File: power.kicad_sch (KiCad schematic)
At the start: 53 parts, among them J1 USB_C_Receptacle_USB2.0_14P, Q2 Q_NMOS_GDS, SW2 SW_SPDT, U16 74LVC1G125, U2 BQ25895RTW, U4 LM1117DT-3.3, U5 MCP4017-xxxxLT, U7 LM3478MA

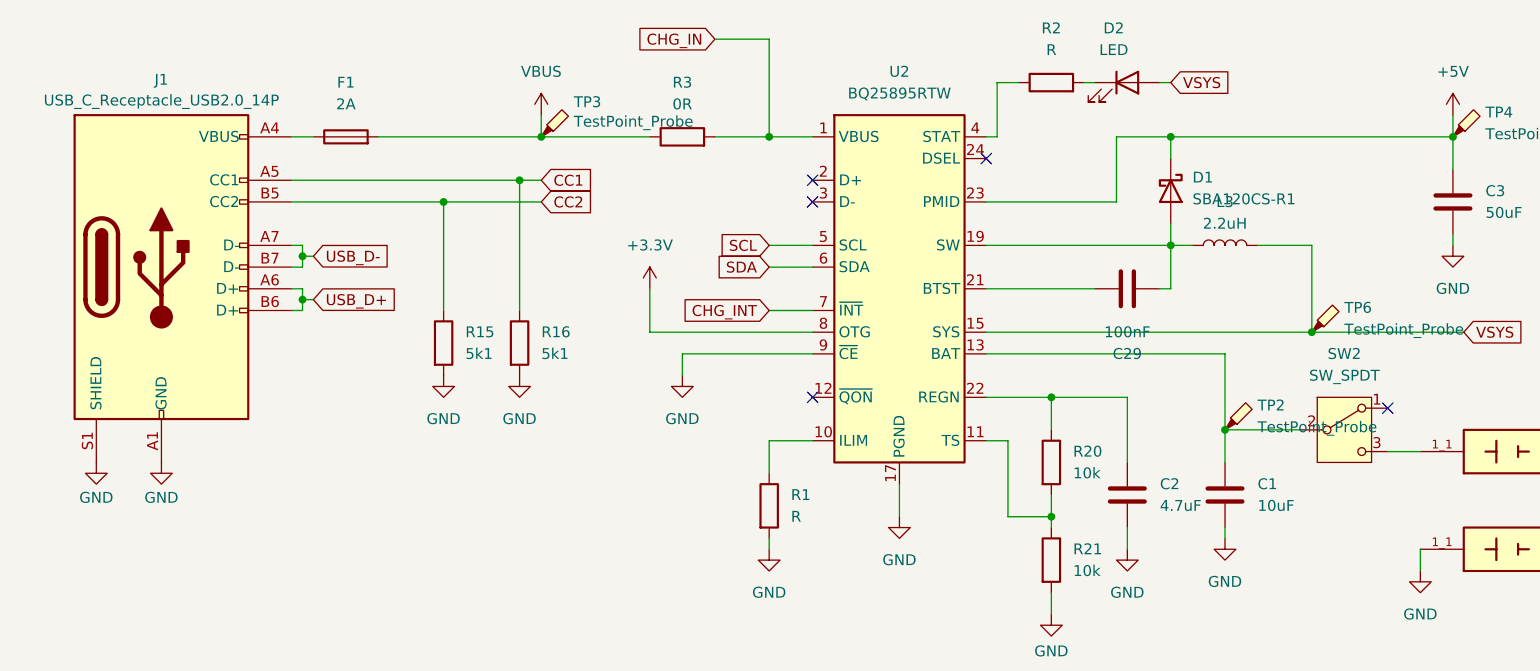
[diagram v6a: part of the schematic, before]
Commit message: Add mounting holes and put test points
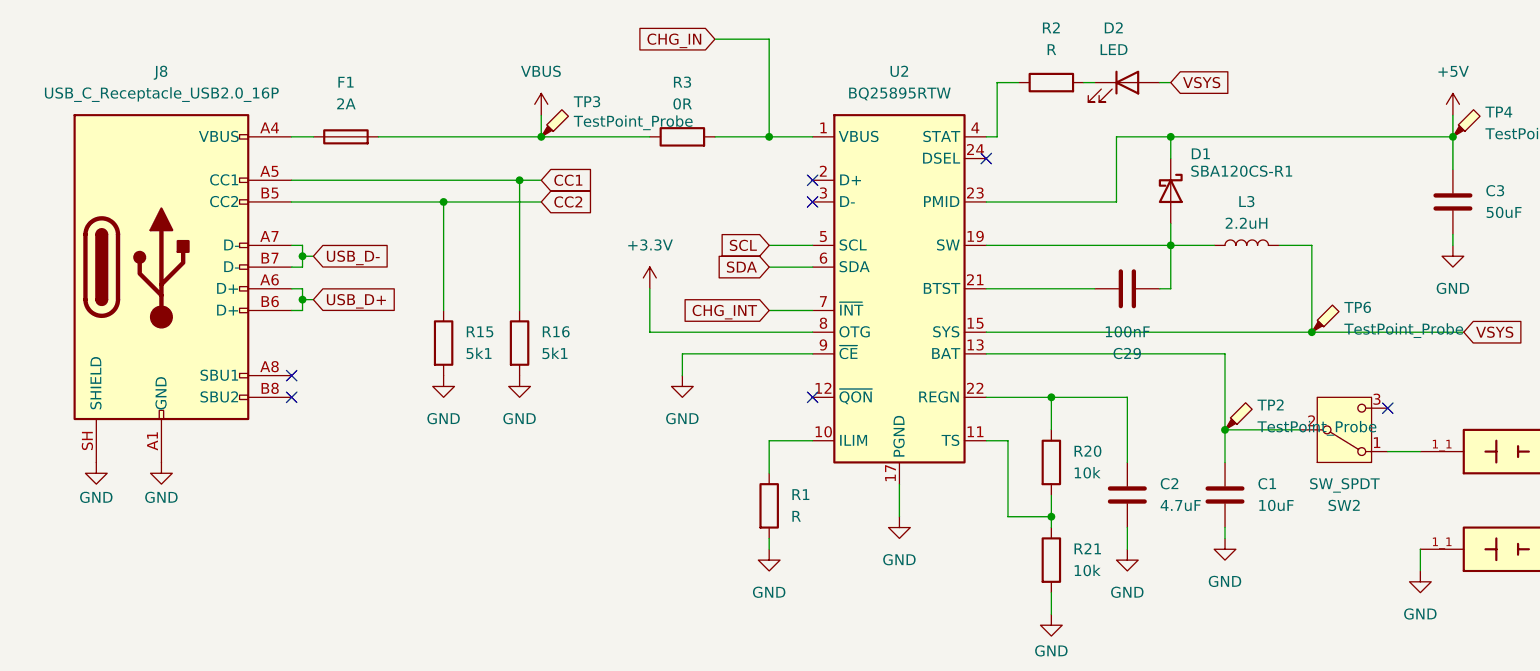
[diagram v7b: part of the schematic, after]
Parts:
- removed J1: USB_C_Receptacle_USB2.0_14P, Connector_USB:USB_C_Receptacle_G-Switch_GT-USB-7010ASV, symbol Connector:USB_C_Receptacle_USB2.0_14P
- added J8: USB_C_Receptacle_USB2.0_16P, Connector_USB:USB_C_Receptacle_G-Switch_GT-USB-7010ASV, symbol Connector:USB_C_Receptacle_USB2.0_16P
- TP2: footprint TestPoint:TestPoint_THTPad_D2.0mm_Drill1.0mm -> TestPoint:TestPoint_Pad_D2.0mm
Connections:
- net CC1: now also J8.A5 (CC1)
- net CC2: now also J8.B5 (CC2)
- net GND: now also J8.A1 (GND), J8.A12 (GND), J8.B1 (GND), J8.B12 (GND), J8.SH (SHIELD)
- net USB_D+: now also J8.A6 (D+), J8.B6 (D+)
- net USB_D-: now also J8.A7 (D-), J8.B7 (D-)
- net at SW2.1 (A): now also BT1.1_1, BT1.1_2, BT1.1_3
- net at F1.1: now also J8.A4 (VBUS), J8.A9 (VBUS), J8.B4 (VBUS), J8.B9 (VBUS)
- now unconnected: SW2.3 (C)
- no-connect marks 6 -> 8
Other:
- moved on the sheet: L3
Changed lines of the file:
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@@
 	)
 	(no_connect
+		(at 48.26 60.96)
+	)
+	(no_connect
 		(at 109.22 60.96)
 	)
@@
 	)
 	(no_connect
+		(at 48.26 58.42)
+	)
+	(no_connect
 		(at 166.37 139.7)
 	)
@@
 	(wire
 		(pts
-			(xy 167.64 43.18) (xy 161.29 43.18)
+			(xy 167.64 43.18) (xy 163.83 43.18)
 		)
 		(stroke
@@
 	(wire
 		(pts
-			(xy 151.13 43.18) (xy 153.67 43.18)
+			(xy 151.13 43.18) (xy 156.21 43.18)
 		)
 		(stroke
@@
 		(in_pos_files yes)
 		(dnp no)
-		(fields_autoplaced yes)
 		(property "Reference" "D1"
-			(at 153.67 35.2424 90)
+			(at 153.416 32.512 90)
 			(show_name no)
 			(do_not_autoplace no)
@@
 		)
 		(property "Value" "SBA120CS-R1"
-			(at 153.67 37.7824 90)
+			(at 153.416 34.544 90)
 			(show_name no)
 			(do_not_autoplace no)
@@
 			)
 		)
-		(property "Footprint" "TestPoint:TestPoint_THTPad_D2.0mm_Drill1.0mm"
+		(property "Footprint" "TestPoint:TestPoint_Pad_D2.0mm"
 			(at 162.56 64.77 0)
 			(hide yes)
@@
 		(lib_id "Switch:SW_SPDT")
 		(at 171.45 64.77 0)
+		(mirror x)
 		(unit 1)
 		(body_style 1)
@@
 		(in_pos_files yes)
 		(dnp no)
-		(fields_autoplaced yes)
 		(property "Reference" "SW2"
-			(at 171.45 55.88 0)
+			(at 171.45 73.66 0)
 			(show_name no)
 			(do_not_autoplace no)
@@
 		)
 		(property "Value" "SW_SPDT"
-			(at 171.45 58.42 0)
+			(at 171.45 71.12 0)
 			(show_name no)
 			(do_not_autoplace no)
@@
 		)
 		(property "Datasheet" ""
-			(at 171.45 72.39 0)
+			(at 171.45 57.15 0)
 			(hide yes)
 			(show_name no)
@@
 	)
 	(symbol
+		(lib_id "Connector:USB_C_Receptacle_USB2.0_16P")
+		(at 33.02 45.72 0)
+		(unit 1)
+		(body_style 1)
+		(exclude_from_sim no)
+		(in_bom yes)
+		(on_board yes)
+		(in_pos_files yes)
+		(dnp no)
+		(fields_autoplaced yes)
+		(property "Reference" "J8"
+			(at 33.02 22.86 0)
+			(show_name no)
+			(do_not_autoplace no)
+			(effects
+				(font
+					(size 1.27 1.27)
+				)
+			)
+		)
+		(property "Value" "USB_C_Receptacle_USB2.0_16P"
+			(at 33.02 25.4 0)
+			(show_name no)
+			(do_not_autoplace no)
+			(effects
+				(font
+					(size 1.27 1.27)
+				)
+			)
+		)
+		(property "Footprint" "Connector_USB:USB_C_Receptacle_G-Switch_GT-USB-7010ASV"
+			(at 36.83 45.72 0)
+			(hide yes)
+			(show_name no)
+			(do_not_autoplace no)
+			(effects
+				(font
+					(size 1.27 1.27)
+				)
+			)
+		)
+		(property "Datasheet" "https://www.usb.org/sites/default/files/documents/usb_type-c.zip"
+			(at 36.83 45.72 0)
+			(hide yes)
+			(show_name no)
+			(do_not_autoplace no)
+			(effects
+				(font
+					(size 1.27 1.27)
+				)
+			)
+		)
+		(property "Description" "USB 2.0-only 16P Type-C Receptacle connector"
+			(at 33.02 45.72 0)
+			(hide yes)
+			(show_name no)
+			(do_not_autoplace no)
+			(effects
+				(font
+					(size 1.27 1.27)
+				)
+			)
+		)
+		(pin "B9"
+		)
+		(pin "SH"
+		)
+		(pin "A1"
+		)
+		(pin "B8"
+		)
+		(pin "B12"
+		)
+		(pin "B7"
+		)
+		(pin "B6"
+		)
+		(pin "B5"
+		)
+		(pin "B4"
+		)
+		(pin "B1"
+		)
+		(pin "A12"
+		)
+		(pin "A9"
+		)
+		(pin "A8"
+		)
+		(pin "A7"
+		)
+		(pin "A6"
+		)
+		(pin "A5"
+		)
+		(pin "A4"
+		)
+		(instances
+			(project "iw18-hs"
+				(path "/9f21d1c7-829c-4910-99a9-b9bc821490d3/6b4aed28-ff69-41de-bba5-d678791155ce"
+					(reference "J8")
+					(unit 1)
+				)
+			)
+		)
+	)
+	(symbol
 		(lib_id "Device:R")
 		(at 66.04 54.61 0)
@@
 	)
 	(symbol
-		(lib_id "Connector:USB_C_Receptacle_USB2.0_14P")
-		(at 33.02 45.72 0)
-		(unit 1)
-		(body_style 1)
-		(exclude_from_sim no)
-		(in_bom yes)
-		(on_board yes)
-		(in_pos_files yes)
-		(dnp no)
-		(fields_autoplaced yes)
-		(property "Reference" "J1"
-			(at 33.02 23.7955 0)
-			(show_name no)
-			(do_not_autoplace no)
-			(effects
-				(font
-					(size 1.27 1.27)
-				)
-			)
-		)
-		(property "Value" "USB_C_Receptacle_USB2.0_14P"
-			(at 33.02 26.2198 0)
-			(show_name no)
-			(do_not_autoplace no)
-			(effects
-				(font
-					(size 1.27 1.27)
-				)
-			)
-		)
-		(property "Footprint" "Connector_USB:USB_C_Receptacle_G-Switch_GT-USB-7010ASV"
-			(at 36.83 45.72 0)
-			(hide yes)
-			(show_name no)
-			(do_not_autoplace no)
-			(effects
-				(font
-					(size 1.27 1.27)
-				)
-			)
-		)
-		(property "Datasheet" "https://www.usb.org/sites/default/files/documents/usb_type-c.zip"
-			(at 36.83 45.72 0)
-			(hide yes)
-			(show_name no)
-			(do_not_autoplace no)
-			(effects
-				(font
-					(size 1.27 1.27)
-				)
-			)
-		)
-		(property "Description" "USB 2.0-only 14P Type-C Receptacle connector"
-			(at 33.02 45.72 0)
-			(hide yes)
-			(show_name no)
-			(do_not_autoplace no)
-			(effects
-				(font
-					(size 1.27 1.27)
-				)
-			)
-		)
-		(property "TME_SYMBOL" ""
-			(at 33.02 45.72 0)
-			(hide yes)
-			(show_name no)
-			(do_not_autoplace no)
-			(effects
-				(font
-					(size 1.27 1.27)
-				)
-			)
-		)
-		(property "Comment" ""
-			(at 33.02 45.72 0)
-			(hide yes)
-			(show_name no)
-			(do_not_autoplace no)
-			(effects
-				(font
-					(size 1.27 1.27)
-				)
-			)
-		)
-		(pin "B12"
-		)
-		(pin "A7"
-		)
-		(pin "A12"
-		)
-		(pin "B4"
-		)
-		(pin "B1"
-		)
-		(pin "B6"
-		)
-		(pin "A9"
-		)
-		(pin "A1"
-		)
-		(pin "B7"
-		)
-		(pin "A6"
-		)
-		(pin "B9"
-		)
-		(pin "S1"
-		)
-		(pin "B5"
-		)
-		(pin "A4"
-		)
-		(pin "A5"
-		)
-		(instances
-			(project "iw18-hs"
-				(path "/9f21d1c7-829c-4910-99a9-b9bc821490d3/6b4aed28-ff69-41de-bba5-d678791155ce"
-					(reference "J1")
-					(unit 1)
-				)
-			)
-		)
-	)
-	(symbol
 		(lib_id "247:247")
 		(at 190.5 78.74 0)
@@
 	(symbol
 		(lib_id "Device:L")
-		(at 157.48 43.18 90)
+		(at 160.02 43.18 90)
 		(unit 1)
 		(body_style 1)
@@
 		(fields_autoplaced yes)
 		(property "Reference" "L3"
-			(at 157.48 38.1 90)
+			(at 160.02 38.1 90)
 			(show_name no)
 			(do_not_autoplace no)
@@
 		)
 		(property "Value" "2.2uH"
-			(at 157.48 40.64 90)
+			(at 160.02 40.64 90)
 			(show_name no)
 			(do_not_autoplace no)
@@
 		)
 		(property "Footprint" "Inductor_SMD:L_Taiyo-Yuden_NR-50xx"
-			(at 157.48 43.18 0)
+			(at 160.02 43.18 0)
 			(hide yes)
 			(show_name no)
@@
 		)
 		(property "Datasheet" ""
-			(at 157.48 43.18 0)
+			(at 160.02 43.18 0)
 			(hide yes)
 			(show_name no)
@@
 		)
 		(property "Description" "Inductor"
-			(at 157.48 43.18 0)
+			(at 160.02 43.18 0)
 			(hide yes)
 			(show_name no)
@@
 		)
 		(property "TME_SYMBOL" "DJNR5040-2R2-S"
-			(at 157.48 43.18 90)
+			(at 160.02 43.18 90)
 			(hide yes)
 			(show_name no)
@@
 		)
 		(property "Comment" ""
-			(at 157.48 43.18 90)
+			(at 160.02 43.18 90)
 			(hide yes)
 			(show_name no)

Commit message: Plan power planes
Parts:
- added C5: 47uF, Capacitor_SMD:C_0805_2012Metric, symbol Device:C
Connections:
- net GND: now also C5.2
- net VSYS: now also C5.1
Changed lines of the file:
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@@
 	)
 	(junction
+		(at 180.34 53.34)
+		(diameter 0)
+		(color 0 0 0 0)
+	)
+	(junction
 		(at 166.37 142.24)
 		(diameter 0)
@@
 	(wire
 		(pts
+			(xy 180.34 53.34) (xy 185.42 53.34)
+		)
+		(stroke
+			(width 0)
+			(type default)
+		)
+	)
+	(wire
+		(pts
 			(xy 100.33 134.62) (xy 102.87 134.62)
 		)
@@
 	(wire
 		(pts
-			(xy 167.64 53.34) (xy 185.42 53.34)
+			(xy 167.64 53.34) (xy 180.34 53.34)
 		)
 		(stroke
@@
 	)
 	(symbol
+		(lib_id "power:GND")
+		(at 180.34 60.96 0)
+		(unit 1)
+		(body_style 1)
+		(exclude_from_sim no)
+		(in_bom yes)
+		(on_board yes)
+		(in_pos_files yes)
+		(dnp no)
+		(fields_autoplaced yes)
+		(property "Reference" "#PWR0153"
+			(at 180.34 67.31 0)
+			(hide yes)
+			(show_name no)
+			(do_not_autoplace no)
+			(effects
+				(font
+					(size 1.27 1.27)
+				)
+			)
+		)
+		(property "Value" "GND"
+			(at 180.34 66.04 0)
+			(show_name no)
+			(do_not_autoplace no)
+			(effects
+				(font
+					(size 1.27 1.27)
+				)
+			)
+		)
+		(property "Footprint" ""
+			(at 180.34 60.96 0)
+			(hide yes)
+			(show_name no)
+			(do_not_autoplace no)
+			(effects
+				(font
+					(size 1.27 1.27)
+				)
+			)
+		)
+		(property "Datasheet" ""
+			(at 180.34 60.96 0)
+			(hide yes)
+			(show_name no)
+			(do_not_autoplace no)
+			(effects
+				(font
+					(size 1.27 1.27)
+				)
+			)
+		)
+		(property "Description" "Power symbol creates a global label with name \"GND\" , ground"
+			(at 180.34 60.96 0)
+			(hide yes)
+			(show_name no)
+			(do_not_autoplace no)
+			(effects
+				(font
+					(size 1.27 1.27)
+				)
+			)
+		)
+		(pin "1"
+		)
+		(instances
+			(project "iw18-hs"
+				(path "/9f21d1c7-829c-4910-99a9-b9bc821490d3/6b4aed28-ff69-41de-bba5-d678791155ce"
+					(reference "#PWR0153")
+					(unit 1)
+				)
+			)
+		)
+	)
+	(symbol
 		(lib_id "Device:R")
 		(at 93.98 30.48 90)
@@
 					(unit 1)
 				)
+			)
+		)
+	)
+	(symbol
+		(lib_id "Device:C")
+		(at 180.34 57.15 0)
+		(unit 1)
+		(body_style 1)
+		(exclude_from_sim no)
+		(in_bom yes)
+		(on_board yes)
+		(in_pos_files yes)
+		(dnp no)
+		(fields_autoplaced yes)
+		(property "Reference" "C5"
+			(at 184.15 55.8799 0)
+			(show_name no)
+			(do_not_autoplace no)
+			(effects
+				(font
+					(size 1.27 1.27)
+				)
+				(justify left)
+			)
+		)
+		(property "Value" "47uF"
+			(at 184.15 58.4199 0)
+			(show_name no)
+			(do_not_autoplace no)
+			(effects
+				(font
+					(size 1.27 1.27)
+				)
+				(justify left)
+			)
+		)
+		(property "Footprint" "Capacitor_SMD:C_0805_2012Metric"
+			(at 181.3052 60.96 0)
+			(hide yes)
+			(show_name no)
+			(do_not_autoplace no)
+			(effects
+				(font
+					(size 1.27 1.27)
+				)
+			)
+		)
+		(property "Datasheet" ""
+			(at 180.34 57.15 0)
+			(hide yes)
+			(show_name no)
+			(do_not_autoplace no)
+			(effects
+				(font
+					(size 1.27 1.27)
+				)
+			)
+		)
+		(property "Description" "Unpolarized capacitor"
+			(at 180.34 57.15 0)
+			(hide yes)
+			(show_name no)
+			(do_not_autoplace no)
+			(effects
+				(font
+					(size 1.27 1.27)
+				)
+			)
+		)
+		(property "TME_SYMBOL" "AMK212BC6476MG-T"
+			(at 180.34 57.15 0)
+			(hide yes)
+			(show_name no)
+			(do_not_autoplace no)
+			(effects
+				(font
+					(size 1.27 1.27)
+				)
+			)
+		)
+		(pin "2"
+		)
+		(pin "1"
+		)
+		(instances
+			(project "iw18-hs"
+				(path "/9f21d1c7-829c-4910-99a9-b9bc821490d3/6b4aed28-ff69-41de-bba5-d678791155ce"
+					(reference "C5")
+					(unit 1)
+				)
